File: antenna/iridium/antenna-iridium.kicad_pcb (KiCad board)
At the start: 4 copper layers, 60 x 60 mm, 37 parts, among them J1 GSG-USB-MICRO-B-SHIELDED, P1 ANT, P2 CONN_COAX, U1 MGA-61563, U2 EPCOS_DCC6C, U3 ADP151_TSOT, U4 MGA-61563

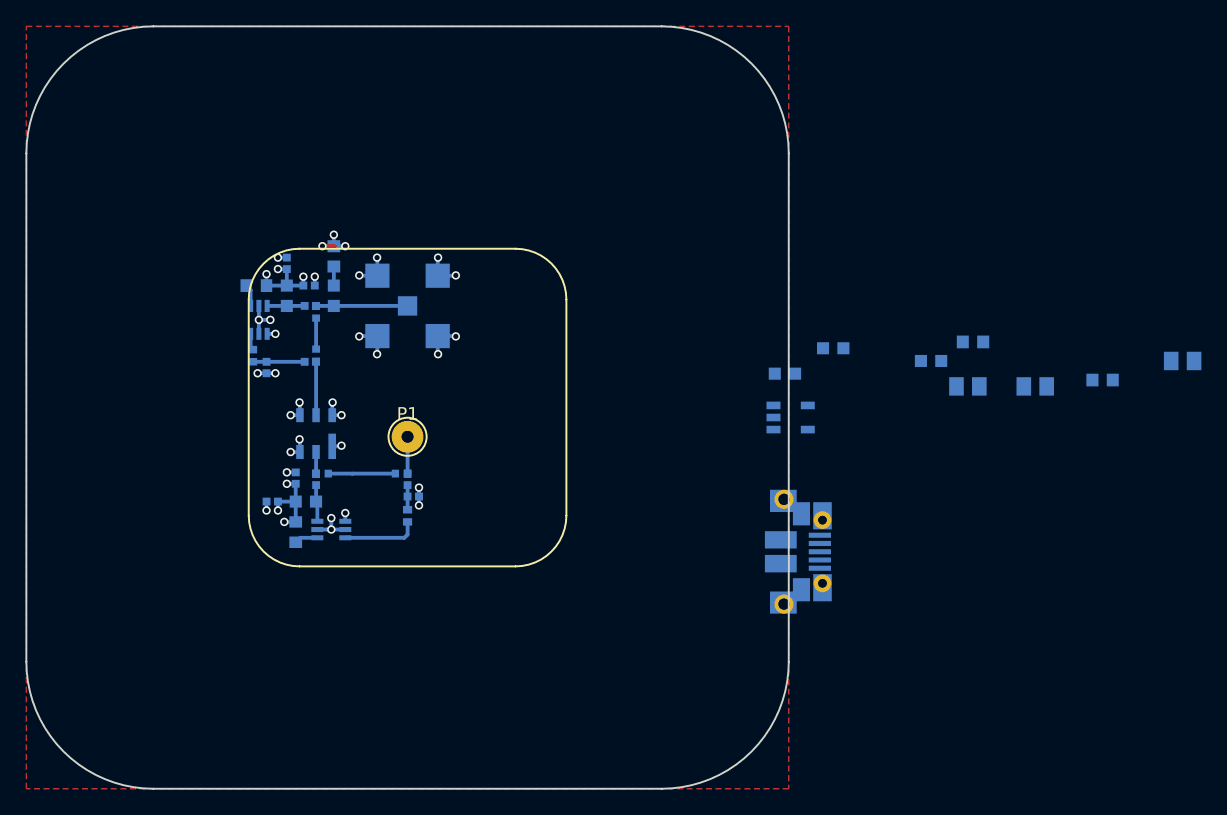
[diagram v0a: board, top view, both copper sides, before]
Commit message: Iridium antenna/filter/LNA routing complete.
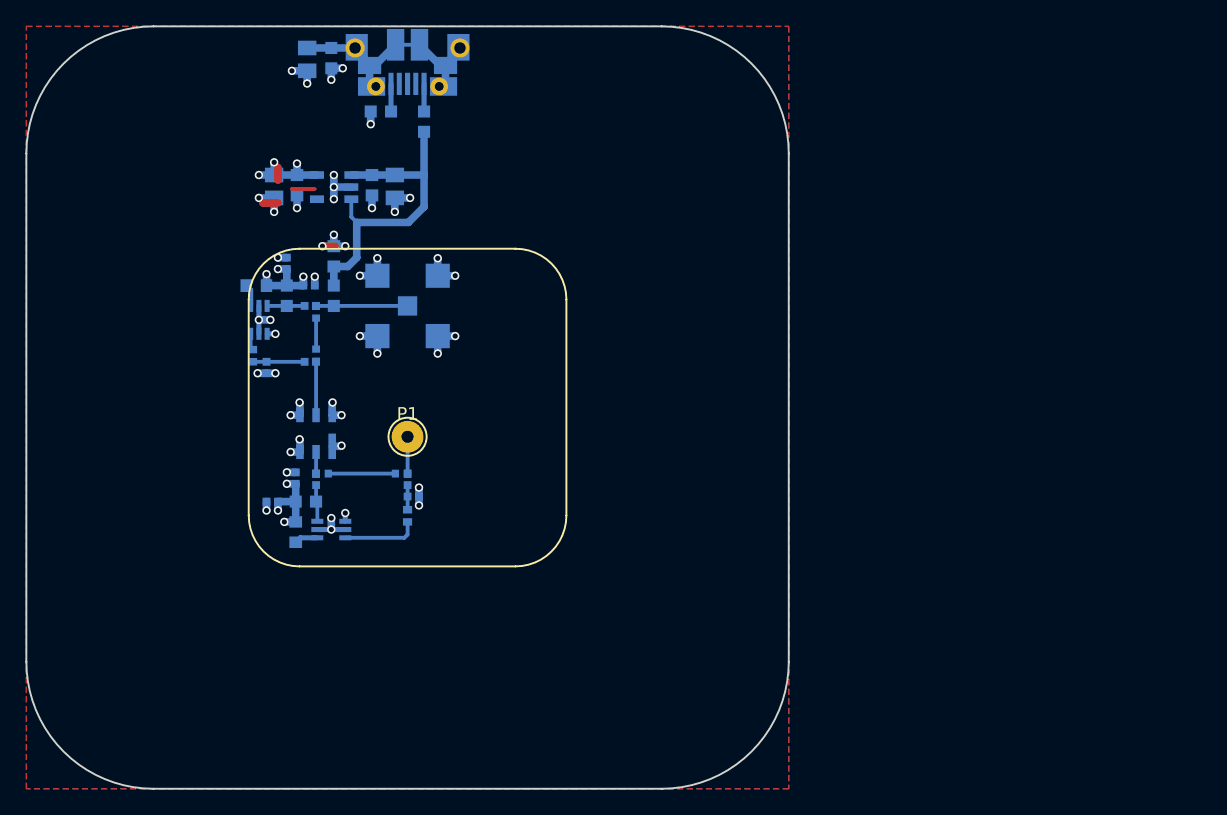
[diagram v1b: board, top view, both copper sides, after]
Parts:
- moved C12 72.8 mm to (139.5, 82.6), turned to 270 degrees
- moved C11 65.2 mm to (141.3, 82.5), turned to 270 degrees
- moved C3 62.8 mm to (142.1, 72.6), turned to 270 degrees
- moved J1 49.9 mm to (150.0, 70.0), turned to 270 degrees
- moved C8 48.9 mm to (147.2, 82.5), turned to 270 degrees
- moved C7 47.8 mm to (149.0, 82.6), turned to 270 degrees
- moved L4 44.1 mm to (151.3, 77.5), turned to 90 degrees
- moved L2 43.5 mm to (144.0, 72.5), turned to 90 degrees
- moved U3 40.2 mm to (144.2, 82.7), turned to 180 degrees
- moved L3 40.2 mm to (147.9, 76.7)
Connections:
- P2 pad 2: (no net) -> GND
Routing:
- net GND: track 22.8 -> 48.7 mm, vias 24 -> 46
- net /V_RAW: track 1.50 -> 25.8 mm
- net Net-(C3-Pad1): track 0.00 -> 18.5 mm
- net (no net): track 11.5 -> 4.00 mm, vias 8 -> 0
- net /V_REG: track 13.2 -> 19.7 mm, vias 6 -> 9
- net Net-(J1-Pad5): track 0.00 -> 2.17 mm
- net Net-(J1-Pad1): track 0.00 -> 2.17 mm
- added copper zone on B.Cu, net GND

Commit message: Silk clean-up/info, copper flood consistency.
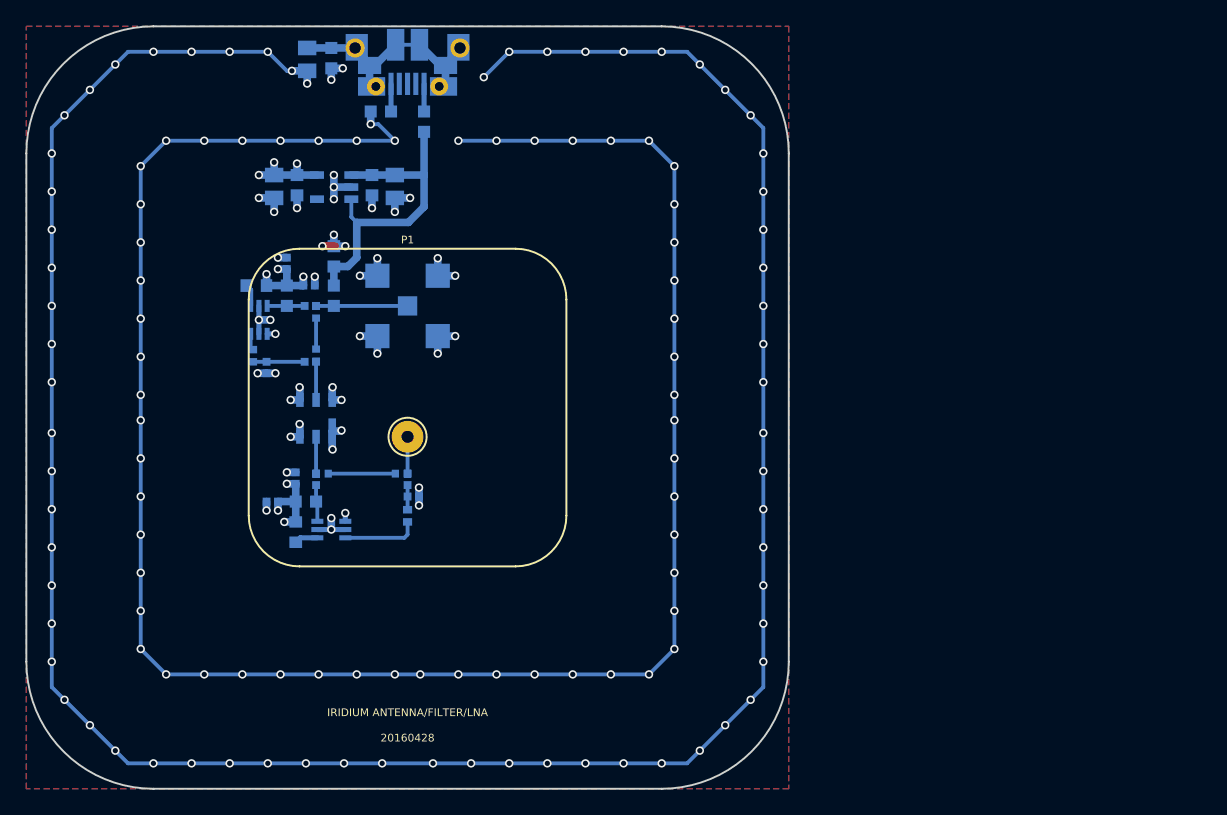
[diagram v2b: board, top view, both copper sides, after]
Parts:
- moved U2 1.20 mm to (142.8, 100.8)
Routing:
- net GND: track 48.7 -> 407.2 mm, vias 46 -> 166
- net (no net): track 4.00 -> 0.00 mm
- net Net-(C6-Pad2): track 1.70 -> 2.90 mm
- net Net-(C9-Pad1): track 4.20 -> 3.00 mm
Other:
- board text added: "20160428"
- board text added: "IRIDIUM ANTENNA/FILTER/LNA"

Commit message: Very minor fixes.
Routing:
- net GND: track 407.2 -> 406.2 mm
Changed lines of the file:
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@@
-(kicad_pcb (version 4) (host pcbnew 4.0.2-stable)
+(kicad_pcb (version 4) (host pcbnew 4.0.2-4+6225~38~ubuntu14.04.1-stable)
   (general
     (links 82)
-    (no_connects 0)
-    (area 119.924999 54.112961 180.075001 130.075001)
+    (no_connects 28)
+    (area 119.924999 69.924999 180.075001 130.075001)
     (thickness 1.6)
     (drawings 10)
-    (tracks 441)
+    (tracks 440)
     (zones 0)
     (modules 37)
@@
       (effects (font (size 0.6096 0.6096) (thickness 0.1524)) (justify mirror))
     )
-    (fp_text value L (at 0 0 90) (layer B.Fab)
+    (fp_text value L (at 0 0 90) (layer B.Fab) hide
       (effects (font (size 0.6096 0.6096) (thickness 0.1524)) (justify mirror))
     )
@@
       (effects (font (size 0.6096 0.6096) (thickness 0.1524)) (justify mirror))
     )
-    (fp_text value L (at 0 0 270) (layer B.Fab)
+    (fp_text value L (at 0 0 270) (layer B.Fab) hide
       (effects (font (size 0.6096 0.6096) (thickness 0.1524)) (justify mirror))
     )
@@
   (segment (start 144.2 87.3) (end 145.1 87.3) (width 0.6) (layer B.Cu) (net 3) (status 10))
   (via (at 145.1 87.3) (size 0.6604) (drill 0.4064) (layers F.Cu B.Cu) (net 3))
-  (segment (start 143.3 87.3) (end 144.3 87.3) (width 0.6) (layer F.Cu) (net 3))
   (segment (start 144.2 87.3) (end 143.3 87.3) (width 0.6) (layer B.Cu) (net 3) (status 10))
   (via (at 143.3 87.3) (size 0.6604) (drill 0.4064) (layers F.Cu B.Cu) (net 3))
@@
     (connect_pads yes (clearance 0.3))
     (min_thickness 0.2)
-    (fill (arc_segments 16) (thermal_gap 0.2) (thermal_bridge_width 0.508))
+    (fill yes (arc_segments 16) (thermal_gap 0.2) (thermal_bridge_width 0.508))
     (polygon
       (pts
@@
     (connect_pads yes (clearance 0.3))
     (min_thickness 0.2)
-    (fill (arc_segments 16) (thermal_gap 0.2) (thermal_bridge_width 0.2))
+    (fill yes (arc_segments 16) (thermal_gap 0.2) (thermal_bridge_width 0.2))
     (polygon
       (pts
@@
     (connect_pads yes (clearance 0.3))
     (min_thickness 0.2)
-    (fill (arc_segments 16) (thermal_gap 0.3) (thermal_bridge_width 0.508))
+    (fill yes (arc_segments 16) (thermal_gap 0.3) (thermal_bridge_width 0.508))
     (polygon
       (pts
@@
     (min_thickness 0.254)
     (keepout (tracks allowed) (vias allowed) (copperpour not_allowed))
-    (fill (arc_segments 16) (thermal_gap 0.508) (thermal_bridge_width 0.508))
+    (fill yes (arc_segments 16) (thermal_gap 0.508) (thermal_bridge_width 0.508))
     (polygon
       (pts
@@
     (min_thickness 0.254)
     (keepout (tracks allowed) (vias allowed) (copperpour not_allowed))
-    (fill (arc_segments 16) (thermal_gap 0.508) (thermal_bridge_width 0.508))
+    (fill yes (arc_segments 16) (thermal_gap 0.508) (thermal_bridge_width 0.508))
     (polygon
       (pts
@@
     (min_thickness 0.254)
     (keepout (tracks allowed) (vias allowed) (copperpour not_allowed))
-    (fill (arc_segments 16) (thermal_gap 0.508) (thermal_bridge_width 0.508))
+    (fill yes (arc_segments 16) (thermal_gap 0.508) (thermal_bridge_width 0.508))
     (polygon
       (pts
@@
     (connect_pads (clearance 0.3))
     (min_thickness 0.2)
-    (fill (arc_segments 16) (thermal_gap 0.2) (thermal_bridge_width 0.3))
+    (fill yes (arc_segments 16) (thermal_gap 0.2) (thermal_bridge_width 0.3))
     (polygon
       (pts
@@
     (min_thickness 0.254)
     (keepout (tracks allowed) (vias allowed) (copperpour not_allowed))
-    (fill (arc_segments 16) (thermal_gap 0.508) (thermal_bridge_width 0.508))
+    (fill yes (arc_segments 16) (thermal_gap 0.508) (thermal_bridge_width 0.508))
     (polygon
       (pts
